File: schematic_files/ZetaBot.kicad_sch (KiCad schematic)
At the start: 16 parts, among them J1 USB C PD Modulle, J2 Conn_01x05, J3 MOTOR_L, J4 MOTOR_R, SW1 SW_SPDT, U1 RPI5, U2 Buck Converter

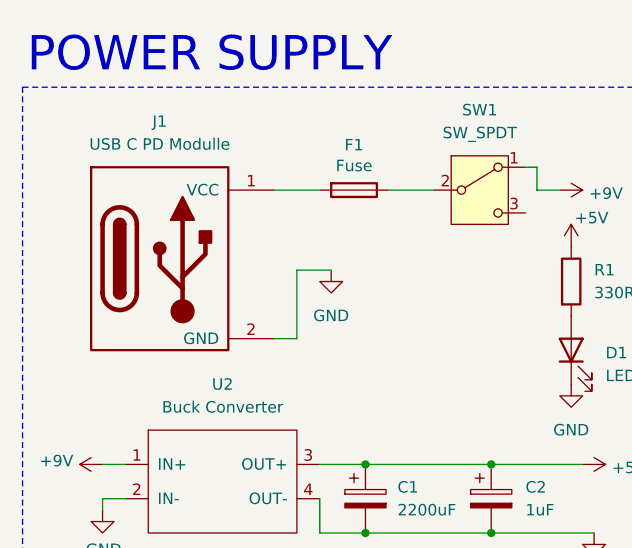
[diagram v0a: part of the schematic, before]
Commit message: Added a new footprint for the USB C PD.
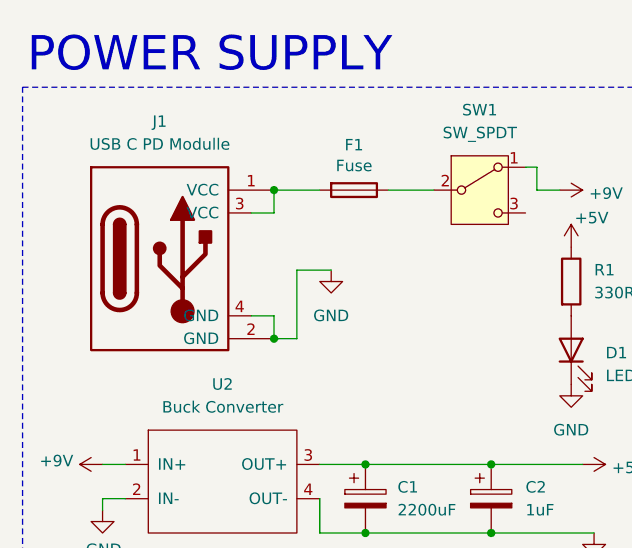
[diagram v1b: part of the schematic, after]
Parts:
- J1: footprint deltabot:USB_C -> DeltaBotFootprints:USB_C; symbol deltabot.lib:USB C PD Connector -> ZetaBot:USB C PD Connector
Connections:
- net GND: now also J1.4 (GND)
- net at F1.2, J1.1 (VCC): now also J1.3 (VCC)
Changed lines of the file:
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@@
 	)
 	(junction
+		(at 41.91 34.29)
+		(diameter 0)
+		(color 0 0 0 0)
+	)
+	(junction
 		(at 63.5 95.25)
 		(diameter 0)
@@
 	)
 	(junction
+		(at 41.91 50.8)
+		(diameter 0)
+		(color 0 0 0 0)
+	)
+	(junction
 		(at 34.29 113.03)
 		(diameter 0)
@@
 	(wire
 		(pts
+			(xy 41.91 48.26) (xy 41.91 50.8)
+		)
+		(stroke
+			(width 0)
+			(type default)
+		)
+	)
+	(wire
+		(pts
 			(xy 176.53 43.18) (xy 167.64 43.18)
 		)
@@
 	(wire
 		(pts
+			(xy 41.91 36.83) (xy 41.91 34.29)
+		)
+		(stroke
+			(width 0)
+			(type default)
+		)
+	)
+	(wire
+		(pts
+			(xy 39.37 48.26) (xy 41.91 48.26)
+		)
+		(stroke
+			(width 0)
+			(type default)
+		)
+	)
+	(wire
+		(pts
 			(xy 66.04 64.77) (xy 76.2 64.77)
 		)
@@
 	(wire
 		(pts
+			(xy 39.37 36.83) (xy 41.91 36.83)
+		)
+		(stroke
+			(width 0)
+			(type default)
+		)
+	)
+	(wire
+		(pts
 			(xy 66.04 72.39) (xy 77.47 72.39)
 		)
@@
 		)
 		(instances
-			(project "EpsilonBot"
+			(project "ZetaBot"
 				(path "/9f04e495-2040-4ae6-9603-65340a735169"
 					(reference "F1")
@@
 		)
 		(instances
-			(project "EpsilonBot"
+			(project "ZetaBot"
 				(path "/9f04e495-2040-4ae6-9603-65340a735169"
 					(reference "#PWR0102")
@@
 		)
 		(instances
-			(project "EpsilonBot"
+			(project "ZetaBot"
 				(path "/9f04e495-2040-4ae6-9603-65340a735169"
 					(reference "#PWR02")
@@
 		)
 		(instances
-			(project "EpsilonBot"
+			(project "ZetaBot"
 				(path "/9f04e495-2040-4ae6-9603-65340a735169"
 					(reference "#PWR03")
@@
 		)
 		(instances
-			(project "EpsilonBot"
+			(project "ZetaBot"
 				(path "/9f04e495-2040-4ae6-9603-65340a735169"
 					(reference "#PWR06")
@@
 		)
 		(instances
-			(project "EpsilonBot"
+			(project "ZetaBot"
 				(path "/9f04e495-2040-4ae6-9603-65340a735169"
 					(reference "#PWR05")
@@
 		)
 		(instances
-			(project "EpsilonBot"
+			(project "ZetaBot"
 				(path "/9f04e495-2040-4ae6-9603-65340a735169"
 					(reference "#PWR09")
@@
 		)
 		(instances
-			(project "EpsilonBot"
+			(project "ZetaBot"
 				(path "/9f04e495-2040-4ae6-9603-65340a735169"
 					(reference "#PWR08")
@@
 		)
 		(instances
-			(project "EpsilonBot"
+			(project "ZetaBot"
 				(path "/9f04e495-2040-4ae6-9603-65340a735169"
 					(reference "J4")
@@
 		)
 		(instances
-			(project "EpsilonBot"
+			(project "ZetaBot"
 				(path "/9f04e495-2040-4ae6-9603-65340a735169"
 					(reference "J3")
@@
 		)
 		(instances
-			(project "EpsilonBot"
+			(project "ZetaBot"
 				(path "/9f04e495-2040-4ae6-9603-65340a735169"
 					(reference "#PWR010")
@@
 		)
 		(instances
-			(project "EpsilonBot"
+			(project "ZetaBot"
 				(path "/9f04e495-2040-4ae6-9603-65340a735169"
 					(reference "#PWR011")
@@
 		)
 		(instances
-			(project "EpsilonBot"
+			(project "ZetaBot"
 				(path "/9f04e495-2040-4ae6-9603-65340a735169"
 					(reference "#PWR012")
@@
 		)
 		(instances
-			(project "EpsilonBot"
+			(project "ZetaBot"
 				(path "/9f04e495-2040-4ae6-9603-65340a735169"
 					(reference "#PWR013")
@@
 		)
 		(instances
-			(project "EpsilonBot"
+			(project "ZetaBot"
 				(path "/9f04e495-2040-4ae6-9603-65340a735169"
 					(reference "#PWR016")
@@
 		)
 		(instances
-			(project "EpsilonBot"
+			(project "ZetaBot"
 				(path "/9f04e495-2040-4ae6-9603-65340a735169"
 					(reference "#PWR018")
@@
 		)
 		(instances
-			(project "EpsilonBot"
+			(project "ZetaBot"
 				(path "/9f04e495-2040-4ae6-9603-65340a735169"
 					(reference "#PWR019")
@@
 		)
 		(instances
-			(project "EpsilonBot"
+			(project "ZetaBot"
 				(path "/9f04e495-2040-4ae6-9603-65340a735169"
 					(reference "#PWR020")
@@
 		)
 		(instances
-			(project "EpsilonBot"
+			(project "ZetaBot"
 				(path "/9f04e495-2040-4ae6-9603-65340a735169"
 					(reference "#PWR021")
@@
 		)
 		(instances
-			(project "EpsilonBot"
+			(project "ZetaBot"
 				(path "/9f04e495-2040-4ae6-9603-65340a735169"
 					(reference "#PWR022")
@@
 		)
 		(instances
-			(project "EpsilonBot"
+			(project "ZetaBot"
 				(path "/9f04e495-2040-4ae6-9603-65340a735169"
 					(reference "#PWR023")
@@
 		)
 		(instances
-			(project "EpsilonBot"
+			(project "ZetaBot"
 				(path "/9f04e495-2040-4ae6-9603-65340a735169"
 					(reference "#PWR01")
@@
 		)
 		(instances
-			(project "EpsilonBot"
+			(project "ZetaBot"
 				(path "/9f04e495-2040-4ae6-9603-65340a735169"
 					(reference "U1")
@@
 		)
 		(instances
-			(project "EpsilonBot"
+			(project "ZetaBot"
 				(path "/9f04e495-2040-4ae6-9603-65340a735169"
 					(reference "#PWR015")
@@
 		)
 		(instances
-			(project "EpsilonBot"
+			(project "ZetaBot"
 				(path "/9f04e495-2040-4ae6-9603-65340a735169"
 					(reference "C6")
@@
 		)
 		(instances
-			(project "EpsilonBot"
+			(project "ZetaBot"
 				(path "/9f04e495-2040-4ae6-9603-65340a735169"
 					(reference "C5")
@@
 		)
 		(instances
-			(project "EpsilonBot"
+			(project "ZetaBot"
 				(path "/9f04e495-2040-4ae6-9603-65340a735169"
 					(reference "J2")
@@
 		)
 		(instances
-			(project "EpsilonBot"
+			(project "ZetaBot"
 				(path "/9f04e495-2040-4ae6-9603-65340a735169"
 					(reference "C2")
@@
 		)
 		(instances
-			(project "EpsilonBot"
+			(project "ZetaBot"
 				(path "/9f04e495-2040-4ae6-9603-65340a735169"
 					(reference "#PWR014")
@@
 		)
 		(instances
-			(project "EpsilonBot"
+			(project "ZetaBot"
 				(path "/9f04e495-2040-4ae6-9603-65340a735169"
 					(reference "R1")
@@
 		)
 		(instances
-			(project "EpsilonBot"
+			(project "ZetaBot"
 				(path "/9f04e495-2040-4ae6-9603-65340a735169"
 					(reference "#PWR07")
@@
 		)
 		(instances
-			(project "EpsilonBot"
+			(project "ZetaBot"
 				(path "/9f04e495-2040-4ae6-9603-65340a735169"
 					(reference "C4")
@@
 	)
 	(symbol
-		(lib_id "deltabot.lib:USB C PD Connector")
+		(lib_id "ZetaBot:USB C PD Connector")
 		(at 31.75 44.45 0)
 		(unit 1)
@@
 			)
 		)
-		(property "Footprint" "deltabot:USB_C"
+		(property "Footprint" "DeltaBotFootprints:USB_C"
 			(at 35.56 41.91 0)
 			(hide yes)
@@
 		(pin "2"
 		)
+		(pin "4"
+		)
+		(pin "3"
+		)
 		(instances
-			(project "EpsilonBot"
+			(project "ZetaBot"
 				(path "/9f04e495-2040-4ae6-9603-65340a735169"
 					(reference "J1")
@@
 		)
 		(instances
-			(project "EpsilonBot"
+			(project "ZetaBot"
 				(path "/9f04e495-2040-4ae6-9603-65340a735169"
 					(reference "D1")
@@
 		)
 		(instances
-			(project "EpsilonBot"
+			(project "ZetaBot"
 				(path "/9f04e495-2040-4ae6-9603-65340a735169"
 					(reference "#PWR025")
@@
 		)
 		(instances
-			(project "EpsilonBot"
+			(project "ZetaBot"
 				(path "/9f04e495-2040-4ae6-9603-65340a735169"
 					(reference "SW1")
@@
 		)
 		(instances
-			(project "EpsilonBot"
+			(project "ZetaBot"
 				(path "/9f04e495-2040-4ae6-9603-65340a735169"
 					(reference "U2")
@@
 		)
 		(instances
-			(project "EpsilonBot"
+			(project "ZetaBot"
 				(path "/9f04e495-2040-4ae6-9603-65340a735169"
 					(reference "C1")
@@
 		)
 		(instances
-			(project "EpsilonBot"
+			(project "ZetaBot"
 				(path "/9f04e495-2040-4ae6-9603-65340a735169"
 					(reference "C3")
